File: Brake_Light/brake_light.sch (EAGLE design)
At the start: 88 parts, among them IC1 LM556D, T2 2SC1307, X1 PWR

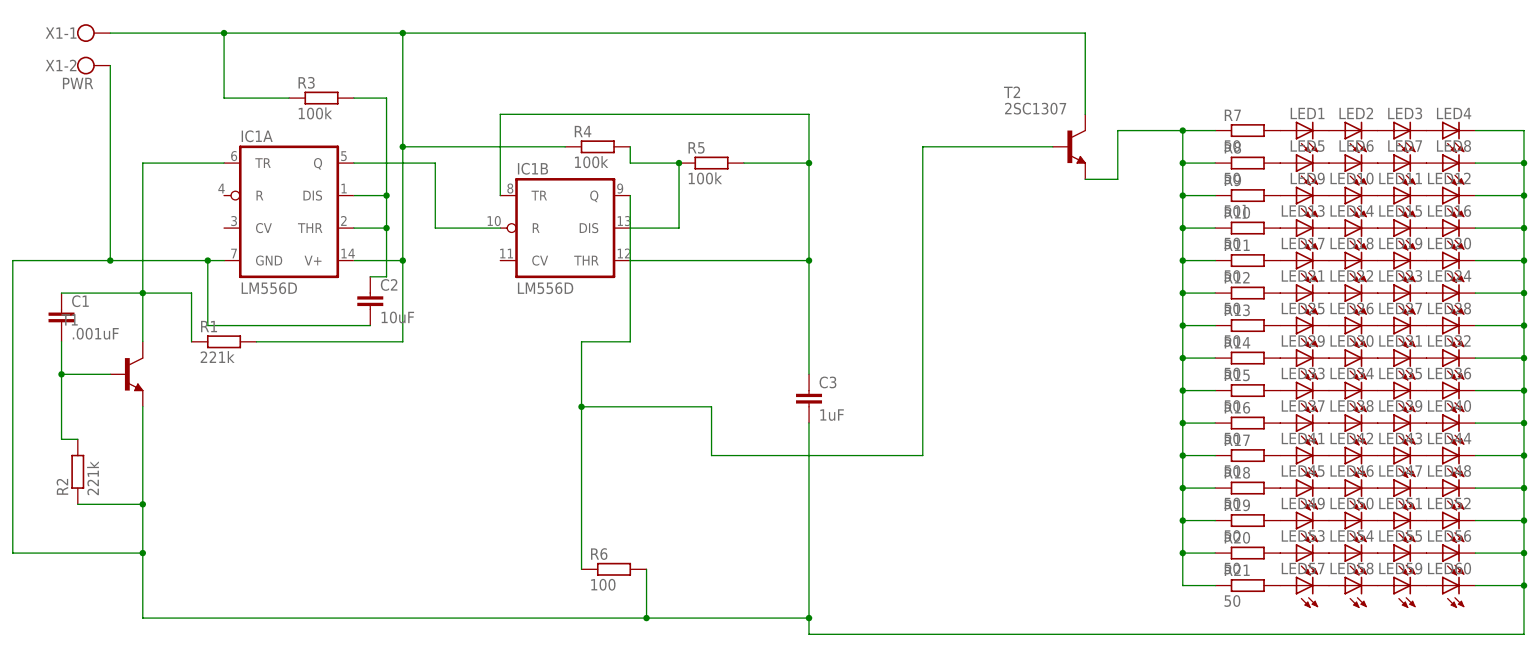
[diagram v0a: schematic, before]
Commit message: Switched to a simpler design
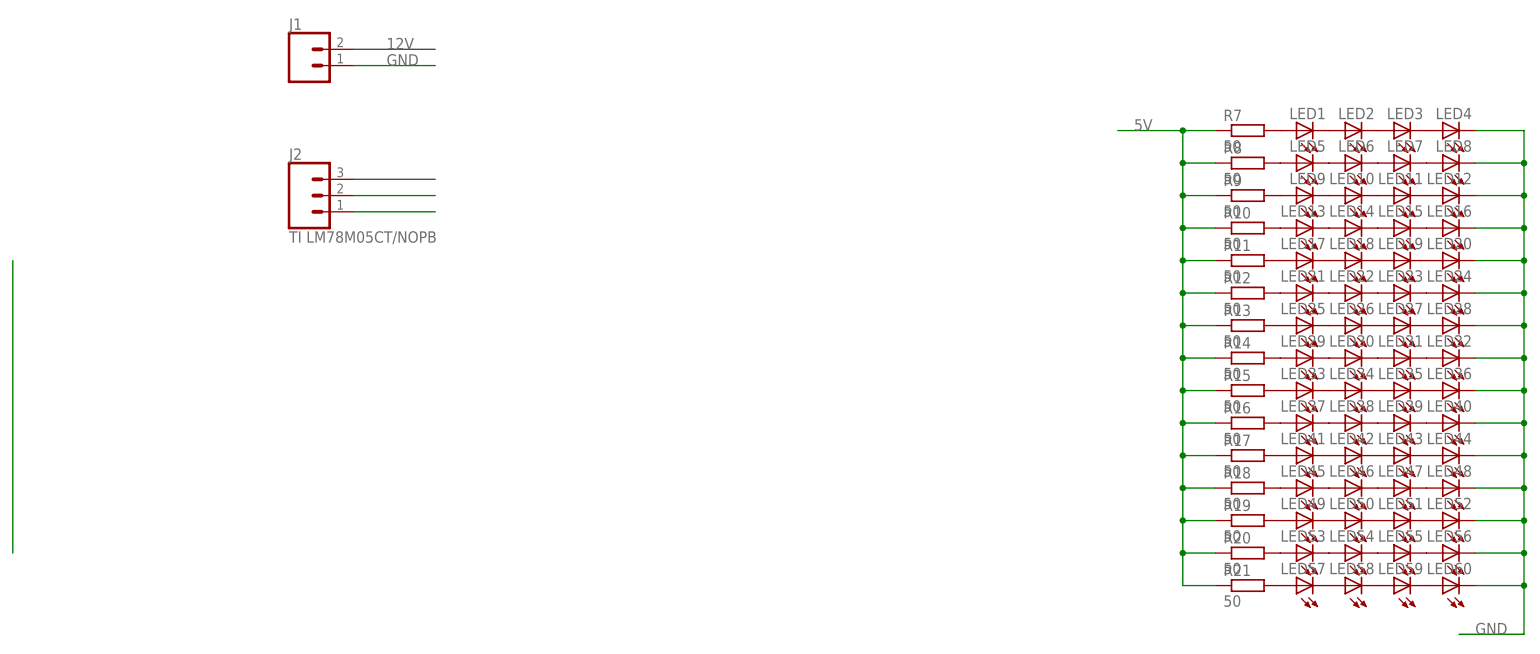
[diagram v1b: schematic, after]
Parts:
- removed C1: .001uF, eagle-ltspice:CC0603
- removed C2: 10uF, eagle-ltspice:C
- removed C3: 1uF, eagle-ltspice:C
- removed IC1: LM556D, linear:LM556D
- removed R1, R2: 221k, eagle-ltspice:R
- removed R3, R4, R5: 100k, eagle-ltspice:R
- removed R6: 100, eagle-ltspice:R
- removed T1: (no value), transistor:-NPN-TO92-EBC
- removed T2: 2SC1307, transistor:2SC1307
- removed X1: PWR, con-wago-500:W237-102
- added J1: (no value), SparkFun-Connectors:CONN_02
- added J2: TI LM78M05CT/NOPB, SparkFun-Connectors:CONN_03
- R10, R11, R12, R13, R14, R15, R16, R17, R18, R19, R20, R21, R7, R8: device eagle-ltspice:R -> eagle-ltspice:RR1206
- R9: value 50] -> 50; device eagle-ltspice:R -> eagle-ltspice:RR1206
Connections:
- removed net N$1: C2.1, IC1A.DIS, IC1A.THR, R3.2
- removed net N$2: IC1A.Q, IC1B.R
- removed net N$3: C1.1, IC1A.TR, R1.1, T1.C
- removed net N$4: C1.2, R2.2, T1.B
- removed net N$6: C3.1, IC1B.THR, IC1B.TR, R5.2
- removed net N$7: IC1B.DIS, R4.2, R5.1
- removed net N$8: IC1B.Q, R6.1, T2.B
- removed net N$9: R10.1, R11.1, R12.1, R13.1, R14.1, R15.1, R16.1, R17.1, R18.1, R19.1, R20.1, R21.1, R7.1, R8.1, R9.1, T2.E
- removed net VCC(5V): IC1A.V+, R1.2, R3.1, R4.1, T2.C, X1-1.KL
- new net 12V: J1.2, J2.1
- new net 5V: J2.3, R10.1, R11.1, R12.1, R13.1, R14.1, R15.1, R16.1, R17.1, R18.1, R19.1, R20.1, R21.1, R7.1, R8.1, R9.1
- net GND: now also J1.1, J2.2; no longer C2.2, C3.2, IC1A.GND, R2.1, R6.2, T1.E, X1-2.KL
